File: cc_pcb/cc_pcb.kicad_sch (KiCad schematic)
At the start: 57 parts, among them J1 Conn_02x05_Odd_Even, SW1 SW_Push, U1 LD1117S33TR_SOT223, U2 STM32F091RCTx

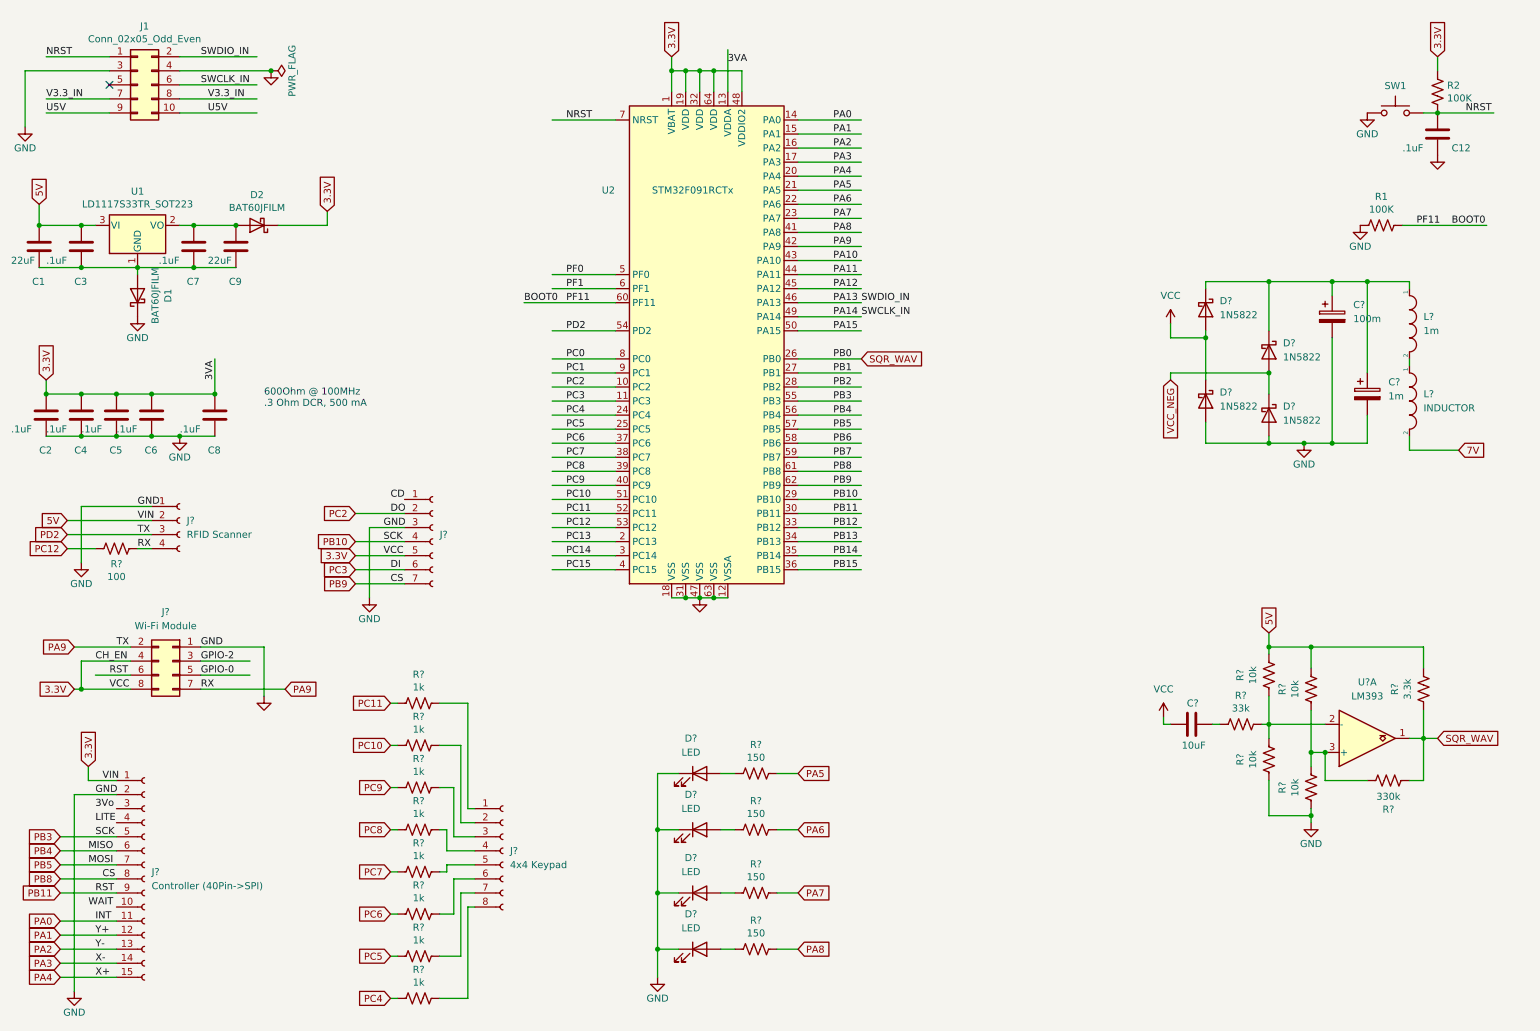
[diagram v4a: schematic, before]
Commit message: ESP8266 footprint and ran electrical check
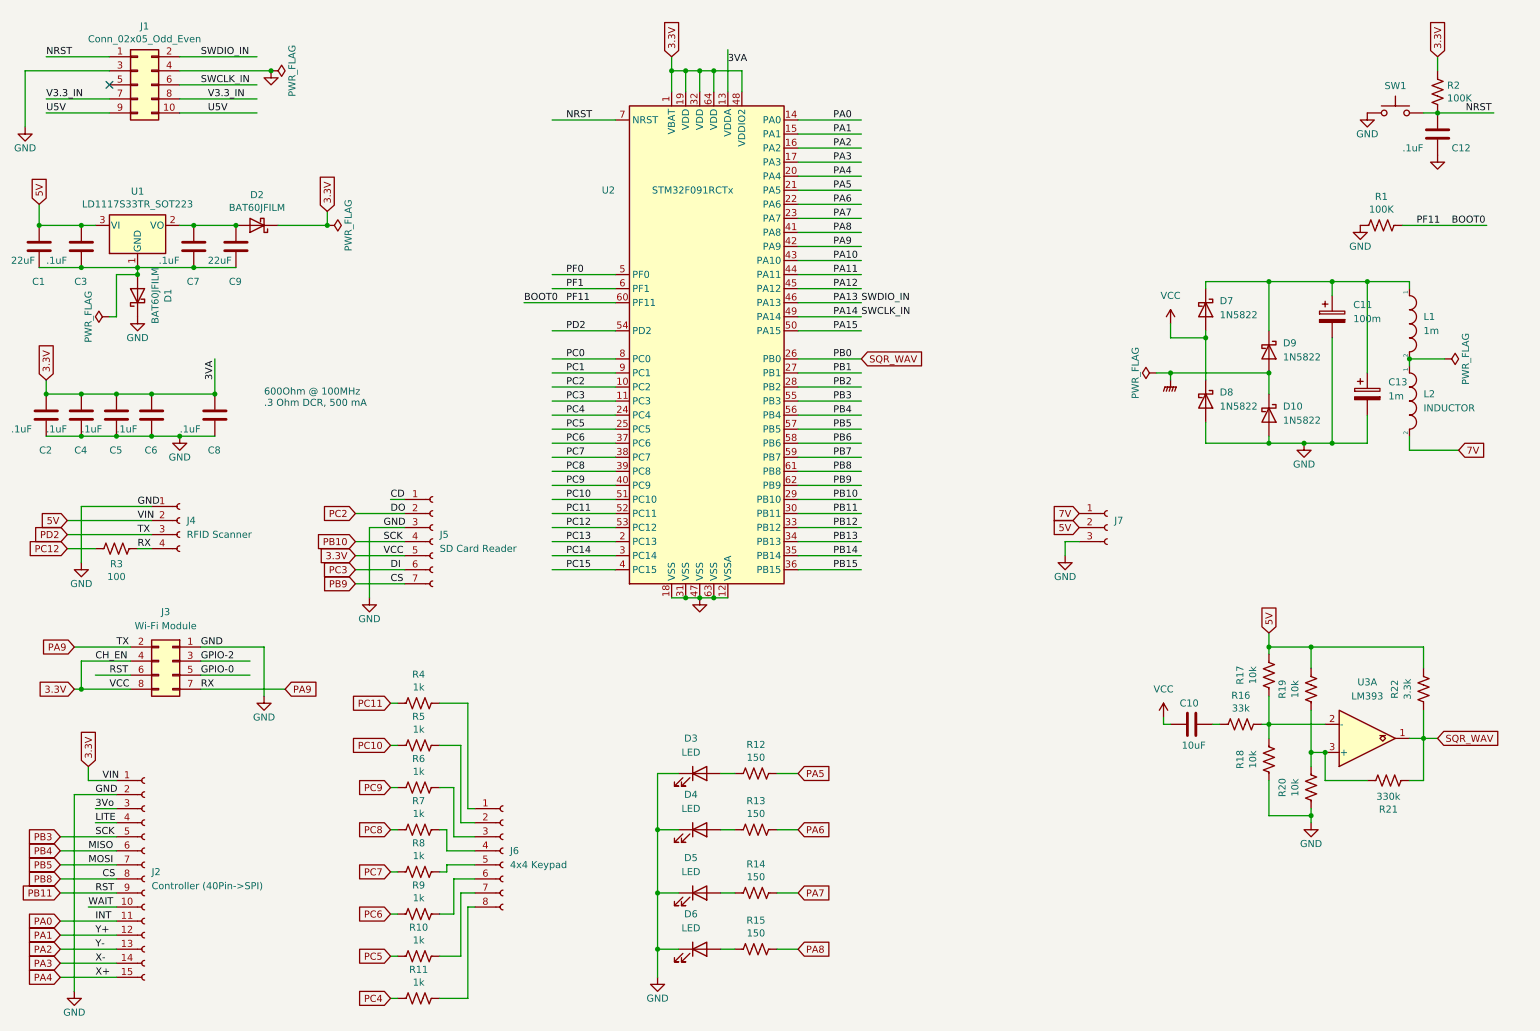
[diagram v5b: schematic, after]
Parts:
- added J7: (no value), symbol Connector:Conn_01x03_Female
- J5: renamed from J?; value (none) -> SD Card Reader; footprint (none) -> imported_footprints:Micro_SD_card_reader
- gave numbers to parts that had none: 38
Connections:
- net 3Vo: now also J2.3 (Pin_3)
- net 7V: now also J7.1 (Pin_1)
- net CD: now also J5.1 (Pin_1)
- net GND: now also J7.3 (Pin_3)
- net LITE: now also J2.4 (Pin_4)
- net VCC: now also J7.2 (Pin_2)
- net WAIT: now also J2.10 (Pin_10)
- net VCC_NEG renamed GNDPWR

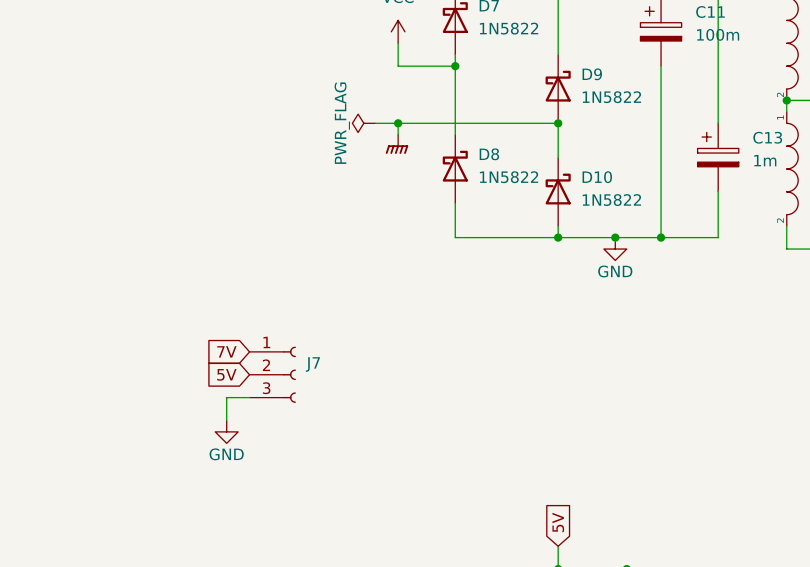
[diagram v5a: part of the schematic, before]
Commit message: able to fill screen of display
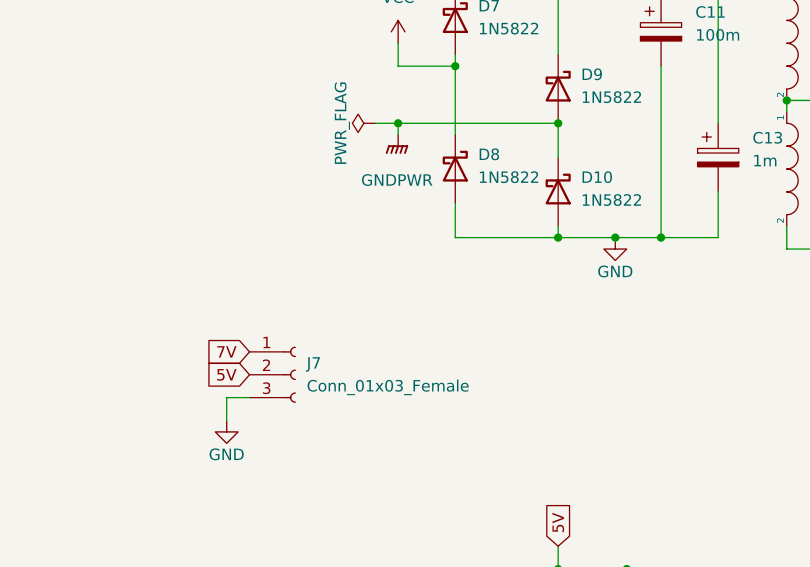
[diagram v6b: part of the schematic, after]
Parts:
- J3: footprint (none) -> imported_footprints:XCVR_ESP8266-01_ESP-01
- J7: value (none) -> Conn_01x03_Female
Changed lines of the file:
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@@
       (effects (font (size 1.27 1.27)) (justify left))
     )
-    (property "Value" "" (id 1) (at 213.36 106.6799 0)
+    (property "Value" "Conn_01x03_Female" (id 1) (at 213.36 106.6799 0)
       (effects (font (size 1.27 1.27)) (justify left))
     )
@@
       (effects (font (size 1.27 1.27)) hide)
     )
-    (property "Value" "" (id 1) (at 223.393 83.82 0))
+    (property "Value" "GNDPWR" (id 1) (at 223.393 83.82 0))
     (property "Footprint" "" (id 2) (at 223.52 80.01 0)
       (effects (font (size 1.27 1.27)) hide)
@@
     (property "Reference" "J3" (id 0) (at 41.91 120.65 0))
     (property "Value" "Wi-Fi Module" (id 1) (at 41.91 123.19 0))
-    (property "Footprint" "" (id 2) (at 43.18 129.54 0)
-      (effects (font (size 1.27 1.27)) hide)
-    )
+    (property "Footprint" "imported_footprints:XCVR_ESP8266-01_ESP-01" (id 2) (at 43.18 129.54 0)
+      (effects (font (size 1.27 1.27)) hide)
+    )
